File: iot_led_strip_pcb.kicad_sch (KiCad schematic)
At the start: 19 parts, among them J1 GT-USB-7010ASV, J2 DC-470-2_1GP, J3 DC-470-2_1GP, J5 Conn_01x04, SW1 RESET, SW2 FLASH, U3 ESP-12E

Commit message: initial rev of design
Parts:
- C4: LCSC (none) -> C15850
- D1, D3: LCSC (none) -> C84256
- J2: value DC-470-2_1GP -> 12V PWR; footprint footprint:DC-IN-TH_DC-470-2.1GP -> Connector_BarrelJack:BarrelJack_GCT_DCJ200-10-A_Horizontal
- J3: value DC-470-2_1GP -> 5V PWR; footprint footprint:DC-IN-TH_DC-470-2.1GP -> Connector_BarrelJack:BarrelJack_GCT_DCJ200-10-A_Horizontal
- J5: value Conn_01x04 -> I2C Expansion
- R10, R11, R5, R6, R7: LCSC (none) -> C17414
- R12: value 100 -> 470; LCSC (none) -> C17710
- R13: LCSC (none) -> C17408
- R3, R4: LCSC (none) -> C27834
- SW1, SW2: footprint footprint:SW-SMD_L6.1-W3.5-LS8.0 -> Button_Switch_SMD:SW_SPST_TL3342; LCSC C5117870 -> C318884
- U3: LCSC (none) -> C89297
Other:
- sheet LED_driver ports: added V_{LED5V}; removed none

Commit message: production files
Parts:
- removed U3: ESP-12E, RF_Module:ESP-12E, symbol RF_Module:ESP-12E
- added U2: ESP-12F, RF_Module:ESP-12E, symbol RF_Module:ESP-12F
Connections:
- net +3.3V: now also U2.8 (VCC)
- net EN: now also U2.3 (EN)
- net Earth: now also U2.15 (GND)
- net GPIO0: now also U2.18 (GPIO0)
- net GPIO15: now also U2.16 (GPIO15)
- net GPIO2: now also U2.17 (GPIO2)
- net LED_driver/LED_B: now also U2.5 (GPIO14)
- net LED_driver/LED_G: now also U2.7 (GPIO13)
- net LED_driver/LED_R: now also U2.6 (GPIO12)
- net RX: now also U2.21 (GPIO3/RXD)
- net SCL: now also U2.20 (GPIO5)
- net SDA: now also U2.19 (GPIO4)
- net TX: now also U2.22 (GPIO1/TXD)
- net ~{RST}: now also U2.1 (~{RST})
- net at R13.2: now also U2.4 (GPIO16)

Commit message: library changes, fixed model for dc jack
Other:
- title: IoT LED Strip Driver -> Spotify Reactive IoT LED Strip Driver
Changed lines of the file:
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@@
   (paper "A4")
   (title_block
-    (title "IoT LED Strip Driver")
+    (title "Spotify Reactive IoT LED Strip Driver")
     (date "2023-08-13")
-    (rev "v1.0")
+    (rev "v1.8-a")
     (comment 1 "A modular, internet connected LED strip driver")
+    (comment 2 "that reacts to the currently playing song on spotify")
   )
+  (bus_alias "I2C" (members "SDA" "SCL"))
   (bus_alias "USB" (members "USB_D+" "USB_D-"))
-  (bus_alias "I2C" (members "SDA" "SCL"))
   (junction (at 71.12 53.34) (diameter 0) (color 0 0 0 0)
   )

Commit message: started work on new schematic
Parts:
- removed J2: 12V PWR, Connector_BarrelJack:BarrelJack_GCT_DCJ200-10-A_Horizontal, symbol dc_jack_lib:DC-470-2_1GP
- removed R6: 10k, Resistor_SMD:R_0805_2012Metric_Pad1.20x1.40mm_HandSolder, symbol Device:R_US
- removed U2: ESP-12F, RF_Module:ESP-12E, symbol RF_Module:ESP-12F
- added C10, C17, C7: 100nF, Capacitor_SMD:C_0805_2012Metric_Pad1.18x1.45mm_HandSolder, symbol Device:C
- added C11, C16, C18, C19, C8, C9: 10uF, Capacitor_SMD:C_0805_2012Metric_Pad1.18x1.45mm_HandSolder, symbol Device:C
- added C2, C3: 22pF, Capacitor_SMD:C_0805_2012Metric_Pad1.18x1.45mm_HandSolder, symbol Device:C
- added D5, D6: SMF5V0A, Diode_SMD:D_SMF, symbol Diode:SMF5V0A
- added D8: 1N5819WS, Diode_SMD:D_SOD-323_HandSoldering, symbol Device:D_Schottky
- added FID1, FID2, FID3: Fiducial, Fiducial:Fiducial_0.5mm_Mask1mm, symbol Mechanical:Fiducial
- added H1, H2, H3, H4: MountingHole_Pad, MountingHole:MountingHole_3.2mm_M3_Pad_Via, symbol Mechanical:MountingHole_Pad
- added J6: TC2050-IDC_Cortex-M, Connector:Tag-Connect_TC2050-IDC-FP_2x05_P1.27mm_Vertical, symbol Tag-Connect:TC2050-IDC_Cortex-M
- added JP1: Jumper_2_Bridged, Connector_PinHeader_2.54mm:PinHeader_1x02_P2.54mm_Vertical, symbol Jumper:Jumper_2_Bridged
- added JP2: JTAG-VTREF, Jumper:SolderJumper-2_P1.3mm_Open_RoundedPad1.0x1.5mm, symbol Jumper:SolderJumper_2_Open
- added JP2: USB PWR, Jumper:SolderJumper-2_P1.3mm_Open_RoundedPad1.0x1.5mm, symbol Jumper:SolderJumper_2_Open
- added R8, R9: 470, Resistor_SMD:R_0805_2012Metric_Pad1.20x1.40mm_HandSolder, symbol Device:R_US
- added TP1: D+, TestPoint:TestPoint_Pad_D1.5mm, symbol Connector:TestPoint
- added TP2: D-, TestPoint:TestPoint_Pad_D1.5mm, symbol Connector:TestPoint
- added TP3: RX, TestPoint:TestPoint_Pad_D1.5mm, symbol Connector:TestPoint
- added TP4: TX, TestPoint:TestPoint_Pad_D1.5mm, symbol Connector:TestPoint
- added TP6: 5V, TestPoint:TestPoint_Pad_D2.0mm, symbol Connector:TestPoint
- added TP7: 3.3V, TestPoint:TestPoint_Pad_D2.0mm, symbol Connector:TestPoint
- added TP8: GND, TestPoint:TestPoint_Pad_D2.0mm, symbol Connector:TestPoint
- added U3: ESP32-S2-MINI-1, PCM_Espressif:ESP32-S2-MINI-1, symbol PCM_Espressif:ESP32-S2-MINI-1
- added U5: AMS1117-3.3, Package_TO_SOT_SMD:SOT-223-3_TabPin2, symbol Regulator_Linear:AMS1117-3.3
- added Y1: Crystal_40Mhz, Crystal:Crystal_SMD_3225-4Pin_3.2x2.5mm_HandSoldering, symbol Device:Crystal_GND24
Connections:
- net +3.3V: now also C17.1, C18.1, JP2.1 (A), U3.3 (3V3)
- net Earth: now also C10.2, C11.2, C16.2, C17.2, C18.2, C19.2, C2.2, C3.2, C7.2, C8.2, C9.2, D5.2 (A2), D6.2 (A2), H1.1, H2.1, H3.1, H4.1, J6.3 (GND), TP8.1, U3.1 (GND), U3.2 (GND), U3.30 (GND), U3.42 (GND), U3.43 (GND), U3.46 (GND), U3.47 (GND), U3.48 (GND), U3.49 (GND), U3.50 (GND), U3.51 (GND), U3.52 (GND), U3.53 (GND), U3.54 (GND), U3.55 (GND), U3.56 (GND), U3.57 (GND), U3.58 (GND), U3.59 (GND), U3.60 (GND), U3.61 (GND), U3.62 (GND), U3.63 (GND), U3.64 (GND), U3.65 (GND), U5.1 (GND), Y1.2, Y1.4
- net GPIO0: no longer R11.1, SW2.2
- net RX: now also R8.2, TP3.1
- net TX: now also R9.2, TP4.1
- net USB_D+: now also TP1.1, U3.24 (USB_D+/ADC2_CH9/GPIO20)
- net USB_D-: now also TP2.1, U3.23 (USB_D-/ADC2_CH8/GPIO19)
- net VBUS: now also J6.5 ((GND)/(Vcc5V)), JP1.2 (B), JP2.2 (B)
- net ~{RST}: now also C19.1, J6.10 (nRESET), U3.45 (CHIP/PU/RESET)
- new net: J6.1 (VCC), JP2.2 (B)
- new net 3.3V: C10.1, C11.1, D8.2 (A), TP7.1, U5.2 (VO)
- new net BOOT: R11.1, SW2.2, U3.4 (GPIO0/BOOT)
- new net RXD: R9.1
- new net TCK: J6.4 (SWDCLK/TCK), U3.35 (MTCK/JTAG/GPIO39)
- new net TDI: J6.8 (NC/TDI), U3.37 (MTDI/JTAG/GPIO41)
- new net TDO: J6.6 (SWO/TDO), U3.36 (MTDO/JTAG/GPIO40)
- new net TMS: J6.2 (SWDIO/TMS), U3.38 (MTMS/JTAG/GPIO42)
- new net TXD: R8.1
- new net VDD_5V: C16.1, C7.1, C8.1, C9.1, D5.1 (A1), D6.1 (A1), D8.1 (K), JP1.1 (A), JP2.1 (A), TP6.1, U5.3 (VI)
- new net X0: C2.1, Y1.1
- new net X1: C3.1, Y1.3
- no-connect marks 9 -> 6
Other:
- removed sheet USB_to_Serial
- note added: "* Notice how TX and RX lines are switched"
- note added: "Clock"
- moved on the sheet: C4, D1, J1, J5, R13, R3, R4

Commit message: schematic v1.9 initial rev
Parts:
- removed C16, C8, C9: 10uF, Capacitor_SMD:C_0805_2012Metric_Pad1.18x1.45mm_HandSolder, symbol Device:C
- removed C7: 100nF, Capacitor_SMD:C_0805_2012Metric_Pad1.18x1.45mm_HandSolder, symbol Device:C
- removed D5, D6: SMF5V0A, Diode_SMD:D_SMF, symbol Diode:SMF5V0A
- removed D8: 1N5819WS, Diode_SMD:D_SOD-323_HandSoldering, symbol Device:D_Schottky
- removed FID1, FID2, FID3: Fiducial, Fiducial:Fiducial_0.5mm_Mask1mm, symbol Mechanical:Fiducial
- removed H1, H2, H3, H4: MountingHole_Pad, MountingHole:MountingHole_3.2mm_M3_Pad_Via, symbol Mechanical:MountingHole_Pad
- removed J3: 5V PWR, Connector_BarrelJack:BarrelJack_GCT_DCJ200-10-A_Horizontal, symbol dc_jack_lib:DC-470-2_1GP
- removed JP1: Jumper_2_Bridged, Connector_PinHeader_2.54mm:PinHeader_1x02_P2.54mm_Vertical, symbol Jumper:Jumper_2_Bridged
- removed JP2: USB PWR, Jumper:SolderJumper-2_P1.3mm_Open_RoundedPad1.0x1.5mm, symbol Jumper:SolderJumper_2_Open
- removed R9: 470, Resistor_SMD:R_0805_2012Metric_Pad1.20x1.40mm_HandSolder, symbol Device:R_US
- removed TP3: RX, TestPoint:TestPoint_Pad_D1.5mm, symbol Connector:TestPoint
- removed TP4: TX, TestPoint:TestPoint_Pad_D1.5mm, symbol Connector:TestPoint
- removed TP6: 5V, TestPoint:TestPoint_Pad_D2.0mm, symbol Connector:TestPoint
- removed TP7: 3.3V, TestPoint:TestPoint_Pad_D2.0mm, symbol Connector:TestPoint
- removed TP8: GND, TestPoint:TestPoint_Pad_D2.0mm, symbol Connector:TestPoint
- removed U5: AMS1117-3.3, Package_TO_SOT_SMD:SOT-223-3_TabPin2, symbol Regulator_Linear:AMS1117-3.3
- added J2: Conn_01x03_Socket, Connector_PinHeader_2.54mm:PinHeader_1x03_P2.54mm_Vertical, symbol Connector:Conn_01x03_Socket
- added J3: Barrel_Jack_Switch_Pin3Ring, Connector_BarrelJack:BarrelJack_Wuerth_6941xx301002, symbol Connector:Barrel_Jack_Switch_Pin3Ring
- added J4: Conn_01x03_Socket_Solderwire, Connector_Wire:SolderWire-0.5sqmm_1x03_P4.8mm_D0.9mm_OD2.3mm_Relief, symbol Connector:Conn_01x03_Socket
- added Q2: BSS138, Package_TO_SOT_SMD:SOT-23, symbol Transistor_FET:BSS138
- added R1, R2: 27R, Resistor_SMD:R_0805_2012Metric_Pad1.20x1.40mm_HandSolder, symbol Device:R_US
- added R6: 0R, Resistor_SMD:R_0805_2012Metric_Pad1.20x1.40mm_HandSolder, symbol Device:R_US
- C10: value 100nF -> 47pF; LCSC C49678 -> C1804; Vendor https://www.lcsc.com/product-detail/Multilayer-Ceramic-Capacitors-MLCC-SMD-SMT_FH-Guangdong-Fenghua-Advanced-Tech-0805B104K500NT_C38141.html -> https://www.lcsc.com/product-detail/Multilayer-Ceramic-Capacitors-MLCC-SMD-SMT_FH-Guangdong-Fenghua-Advanced-Tech-0805CG220J500NT_C24658.html
- C11: value 10uF -> 47pF; LCSC C15850 -> C1804; Vendor https://www.lcsc.com/product-detail/Multilayer-Ceramic-Capacitors-MLCC-SMD-SMT_Murata-Electronics-GRM21BR61C106KE15L_C77075.html -> https://www.lcsc.com/product-detail/Multilayer-Ceramic-Capacitors-MLCC-SMD-SMT_FH-Guangdong-Fenghua-Advanced-Tech-0805CG220J500NT_C24658.html
- R5: value 10k -> 0R
- R8: value 470 -> 10k; LCSC C17710 -> C17414; Vendor https://www.lcsc.com/product-detail/Chip-Resistor-Surface-Mount_VO-0805-5-470_C2889528.html -> https://www.lcsc.com/product-detail/Chip-Resistor-Surface-Mount_FOJAN-FRQ0805F1002TS_C5159708.html
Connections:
- net GPIO15 is gone; now on net LV_DIN: R7.2
- net TXD is gone; now on net +5V: R8.1
- net +3.3V: now also R7.1, Q2.1 (G); no longer R5.1
- net +5V: now also J2.1 (Pin_1), J4.1 (Pin_1)
- net 5VDC: now also J3.1
- net Earth: now also J2.3 (Pin_3), J3.2, J3.3, J4.3 (Pin_3); no longer R7.1
- net SCL: now also U3.31 (GPIO35)
- net SDA: now also U3.28 (GPIO33)
- net USB_D+: now also R1.2; no longer J1.A6 (DP1), J1.B6 (DP2)
- net USB_D-: now also R2.2; no longer J1.A7 (DN1), J1.B7 (DN2)
- net X0: now also R5.1, U3.19 (GPIO15/ADC2_CH4/XTAL_32K_P); no longer C2.1, Y1.1
- net X1: now also U3.20 (GPIO16/ADC2_CH5/XTAL_32K_N), R6.2; no longer C3.1, Y1.3
- net LV_DIN: now reaches U3.25 (GPIO21)
- net LV_DIN: now also Q2.2 (S)
- net at U3.6 (GPIO2/ADC1_CH1): now also R13.2
- net 3.3V: no longer names the net of C11.1
- net 3.3V: now also J1.A7 (DN1), J1.B7 (DN2), R2.1; no longer C10.1
- net GPIO2 renamed X0_R
- net X0_R: now also C2.1, Y1.1
- net RX renamed D_{IN}
- net D_{IN}: now also J2.2 (Pin_2), J4.2 (Pin_2), Q2.3 (D)
- new net: C10.1, J1.A6 (DP1), J1.B6 (DP2), R1.1
- new net X1_R: C3.1, R6.1, Y1.3
- no-connect marks 6 -> 28
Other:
- removed sheet LED_driver
- sheet Power_and_board ports: added none; removed 12VDC IN
- note added: "LED Strip Output"
- note removed: "* Notice how TX and RX lines are switched"
- note removed: "Boot Pin States"
- moved on the sheet: C17, C18, C19, C2, C3, C4, D1, J5, R10, R11, R13, SW1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

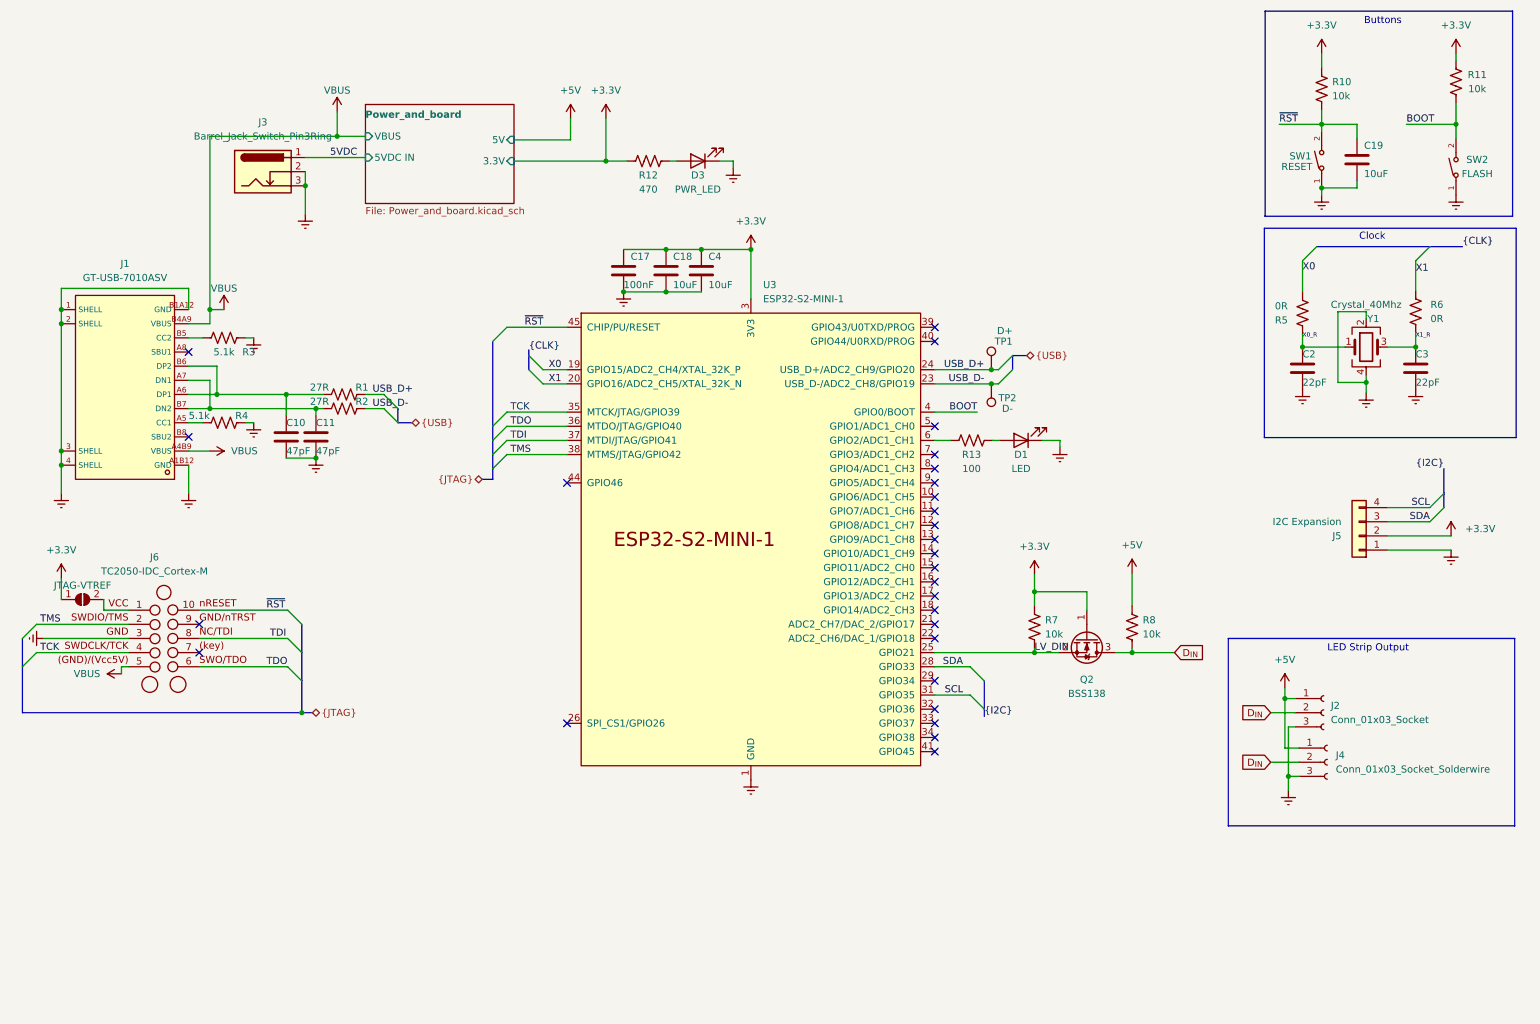
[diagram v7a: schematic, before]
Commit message: some small changes to schematic, cleaned up old pcb
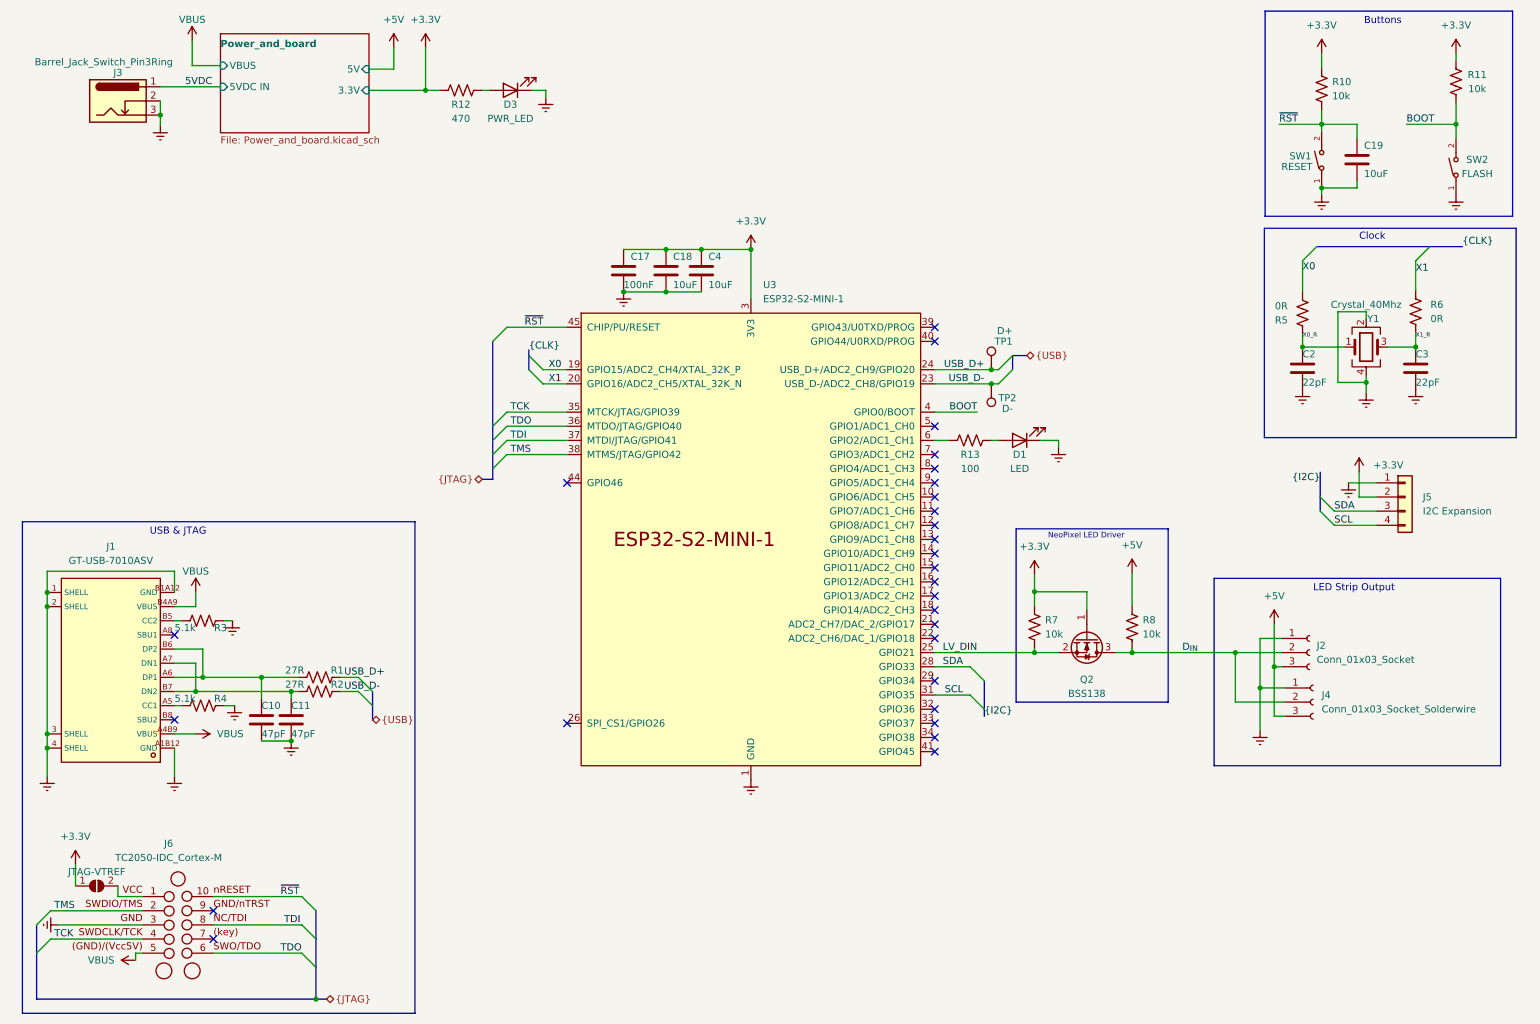
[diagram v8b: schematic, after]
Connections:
- net +5V: now also J2.3 (Pin_3), J4.3 (Pin_3); no longer J2.1 (Pin_1), J4.1 (Pin_1)
- net Earth: now also J2.1 (Pin_1), J4.1 (Pin_1); no longer J2.3 (Pin_3), J4.3 (Pin_3)
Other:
- note added: "NeoPixel LED Driver"
- note added: "USB & JTAG"
- moved on the sheet: C10, C11, D3, J1, J2, J3, J4, J5, J6, R1, R12, R2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
